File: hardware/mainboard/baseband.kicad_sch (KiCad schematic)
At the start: 36 parts, among them U501 MCP4551-103, U502 MCP4551-103, U6 MCP6002, U7 MCP6002

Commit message: Fixed baseband trimming potentiometers MPN
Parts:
- RV2, RV3: MPN 3224W-1-103E -> 3224J-1-103E
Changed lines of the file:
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@@
       (effects (font (size 1.27 1.27)) hide)
     )
-    (property "MPN" "3224W-1-103E" (at 120.65 83.185 0)
+    (property "MPN" "3224J-1-103E" (at 120.65 83.185 0)
       (effects (font (size 1.27 1.27)) hide)
     )
@@
       (effects (font (size 1.27 1.27)) hide)
     )
-    (property "MPN" "3224W-1-103E" (at 102.235 167.64 0)
-      (effects (font (size 1.27 1.27)) hide)
-    )
+    (property "MPN" "3224J-1-103E" (at 102.235 167.64 0)
+      (effects (font (size 1.27 1.27)) hide)
+    )

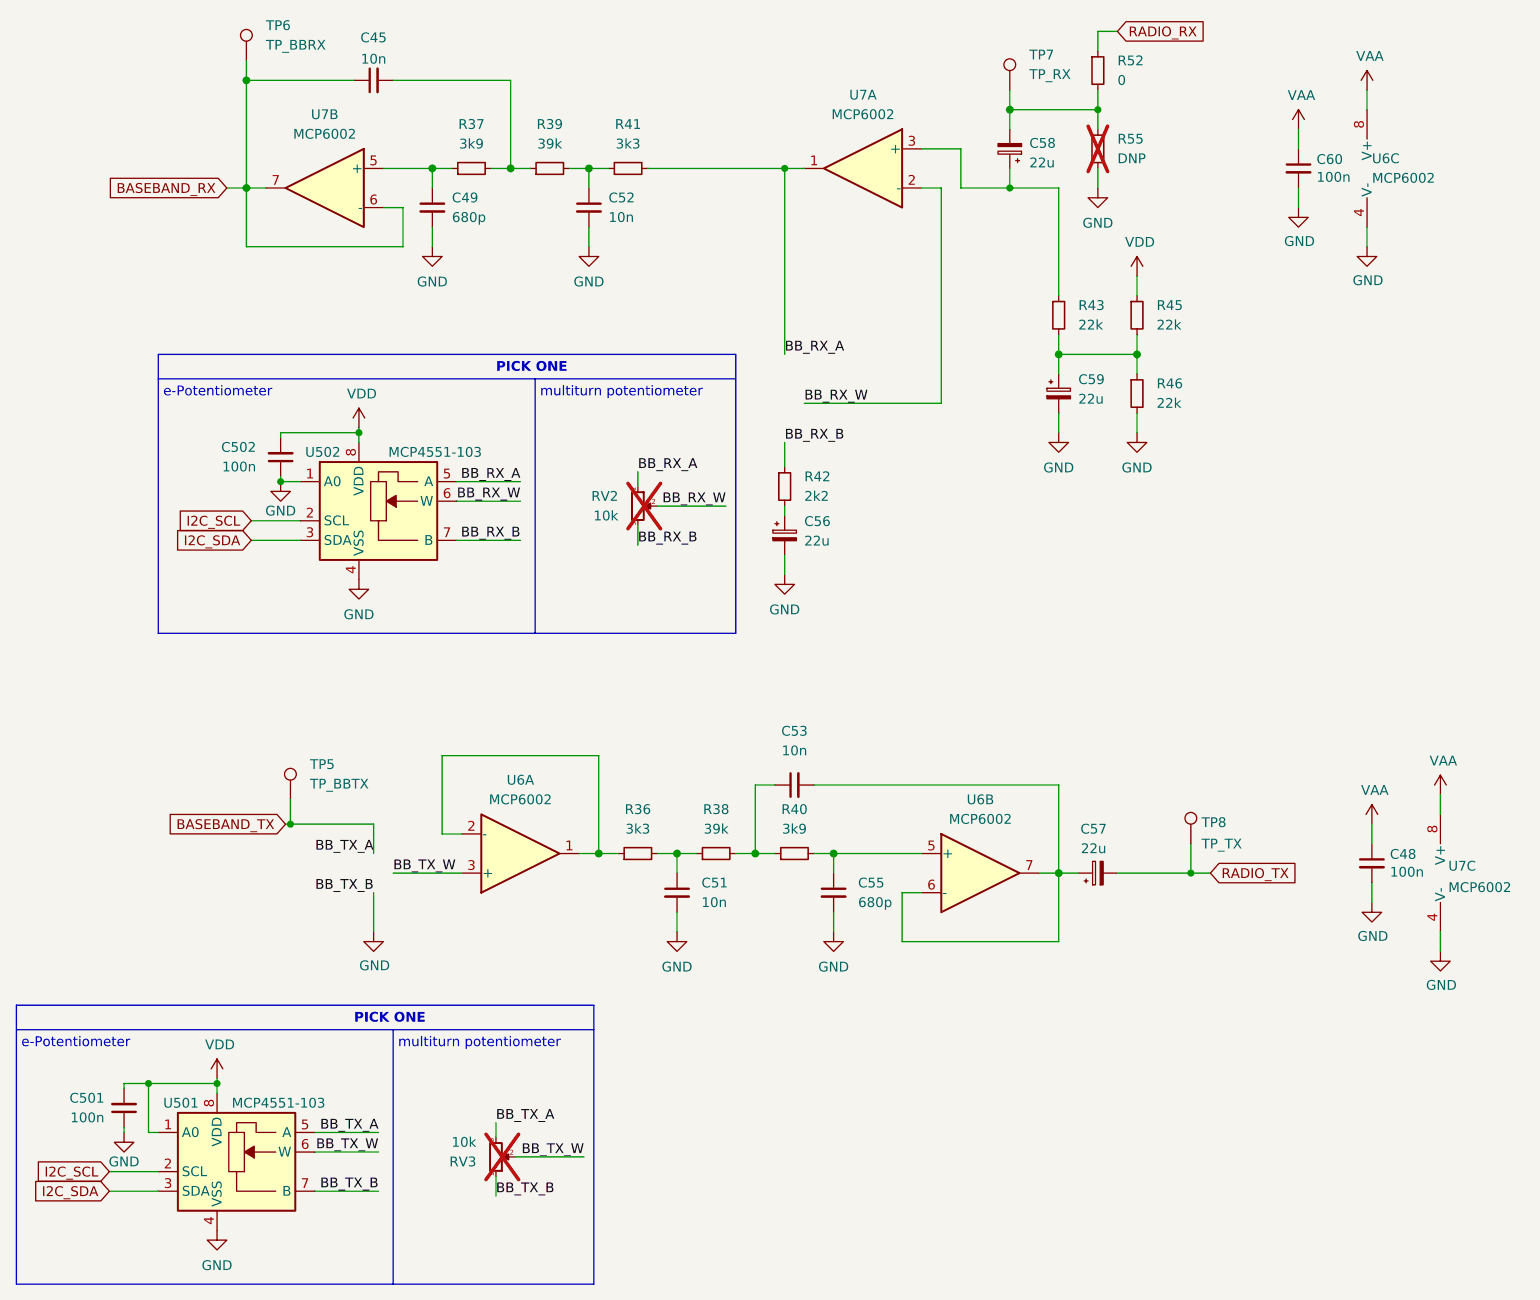
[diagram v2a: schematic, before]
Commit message: Updated mainboard
Replaced OHIS speaker resistors with larger 100 ohms resistors
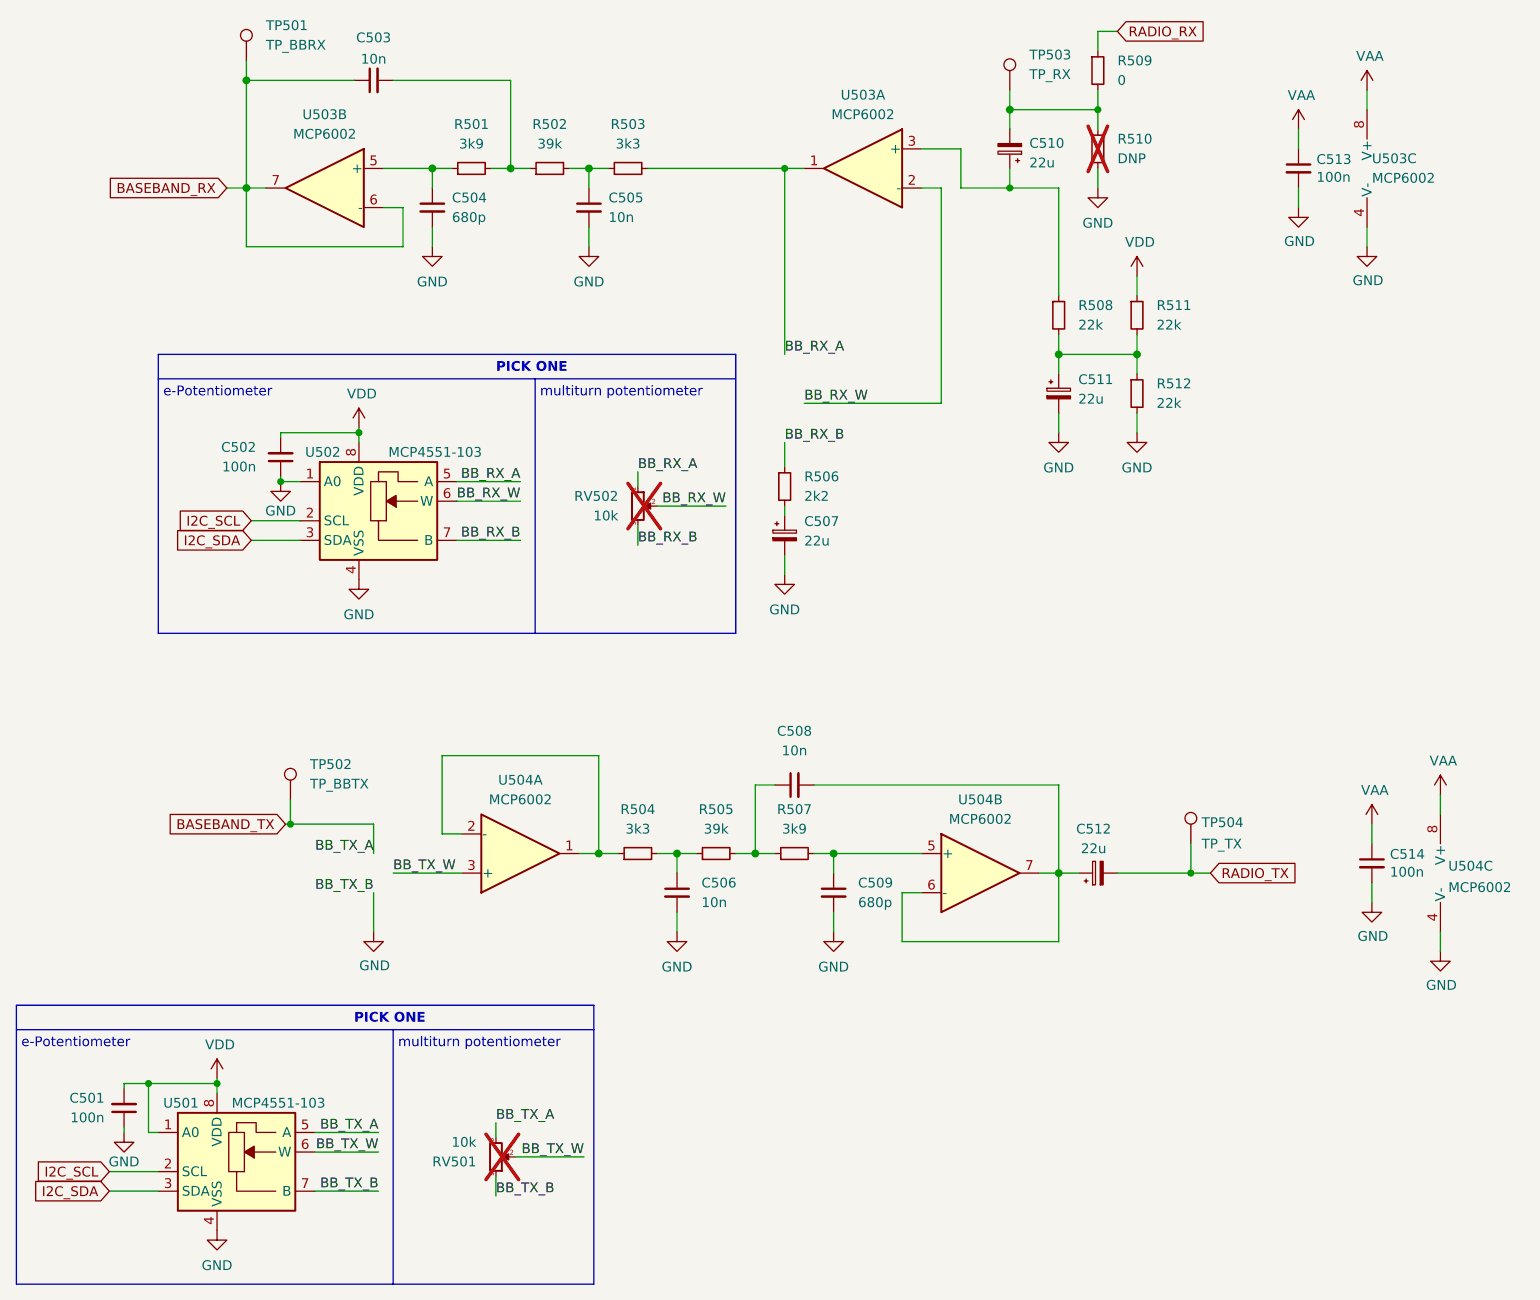
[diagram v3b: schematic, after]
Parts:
- renumbered C45 to C503, C49 to C504, C52 to C505, C51 to C506, C56 to C507, C53 to C508, C55 to C509, C58 to C510, C59 to C511, C57 to C512, C60 to C513, C48 to C514, R37 to R501, R39 to R502, R41 to R503, R36 to R504, R38 to R505, R42 to R506, R40 to R507, R43 to R508, R52 to R509, R55 to R510, R45 to R511, R46 to R512, RV3 to RV501, RV2 to RV502, TP6 to TP501, TP5 to TP502, TP7 to TP503, TP8 to TP504, U7 to U503, U6 to U503, U6 to U504, U7 to U504
